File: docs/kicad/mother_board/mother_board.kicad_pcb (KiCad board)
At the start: 2 copper layers, 148 x 92.5 mm, 37 parts, among them J1 ROW_BOARDS, J10 PEDAL1, J11 PEDAL2, J12 PEDAL3, J13 PEDAL4, J14 GUITAR_IN, J15 LINE_OUT, J16 LEDS, J2 ROTARIES, J3 TE_DISPLAY, J4 RPI_DISPLAY, J5 rPi_5V, J6 RPI_RUN, J7 rpi_connector, J8 I2S_TXB, J9 EigthInchJack1, Q1 BC547, U1 teensyAudioRevD_WithAudio, U2 myTeensy4.1

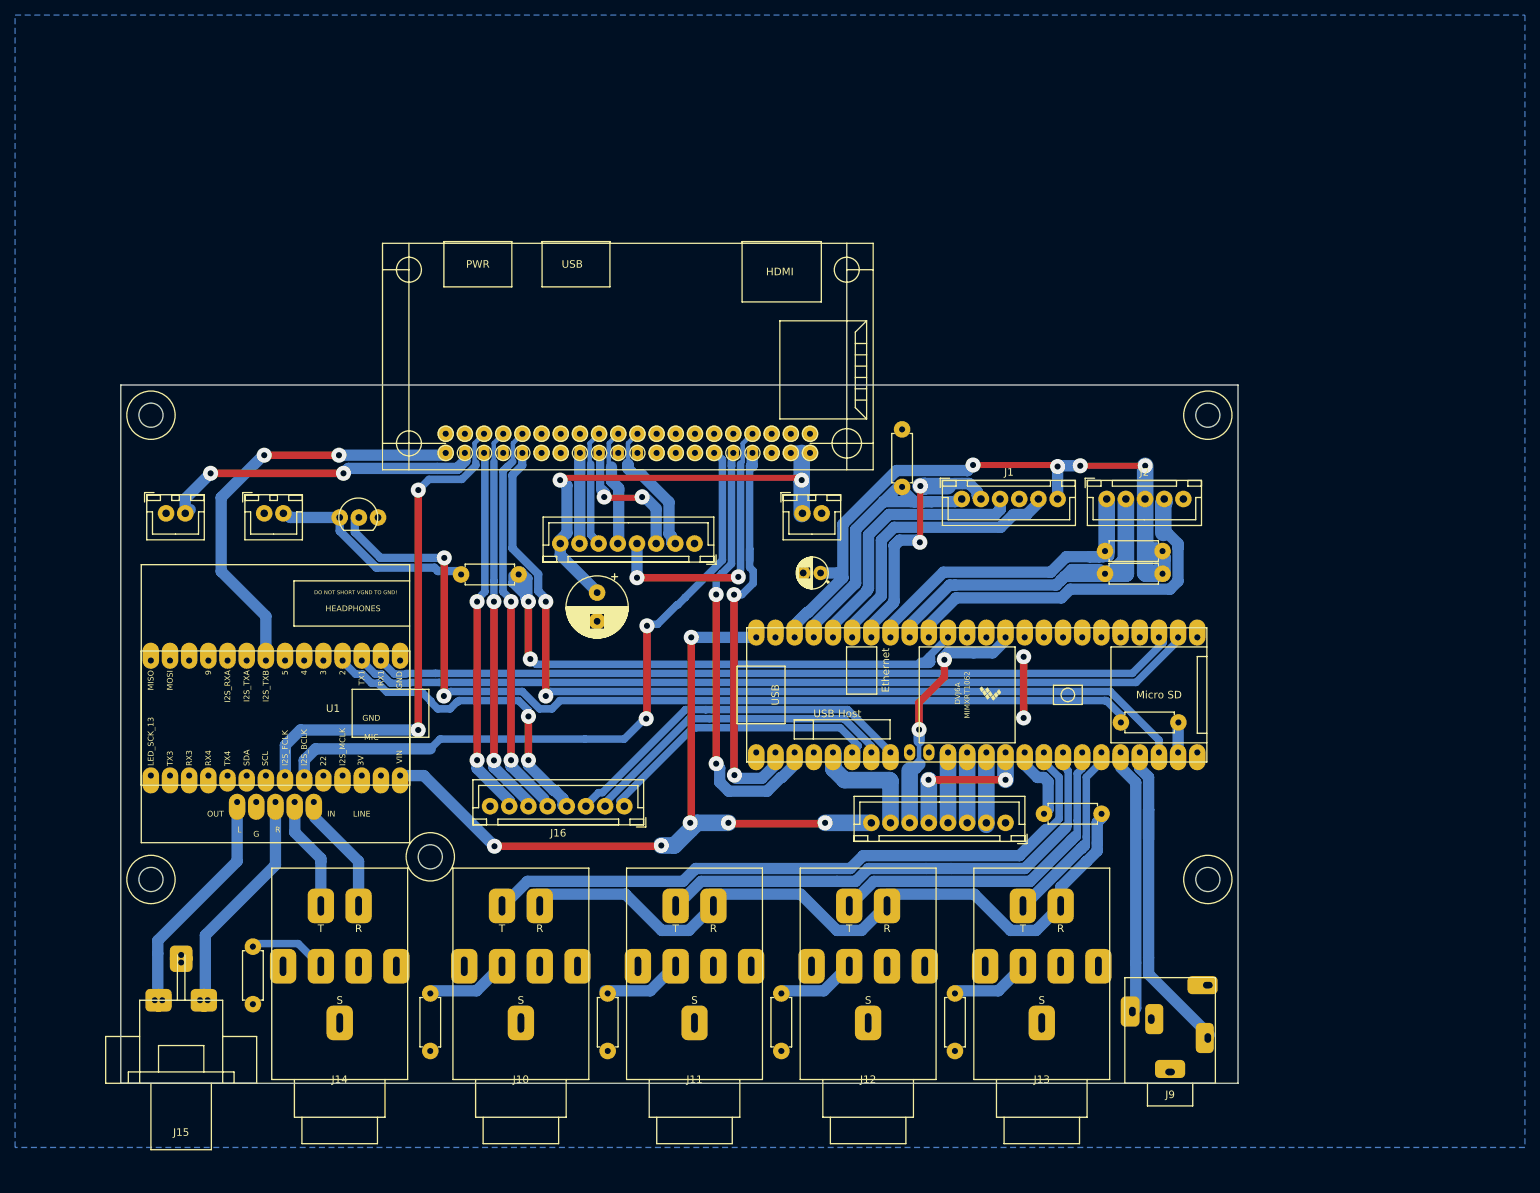
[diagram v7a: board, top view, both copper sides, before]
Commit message: produced and submitted mother_board and row_board to PCBWay for production
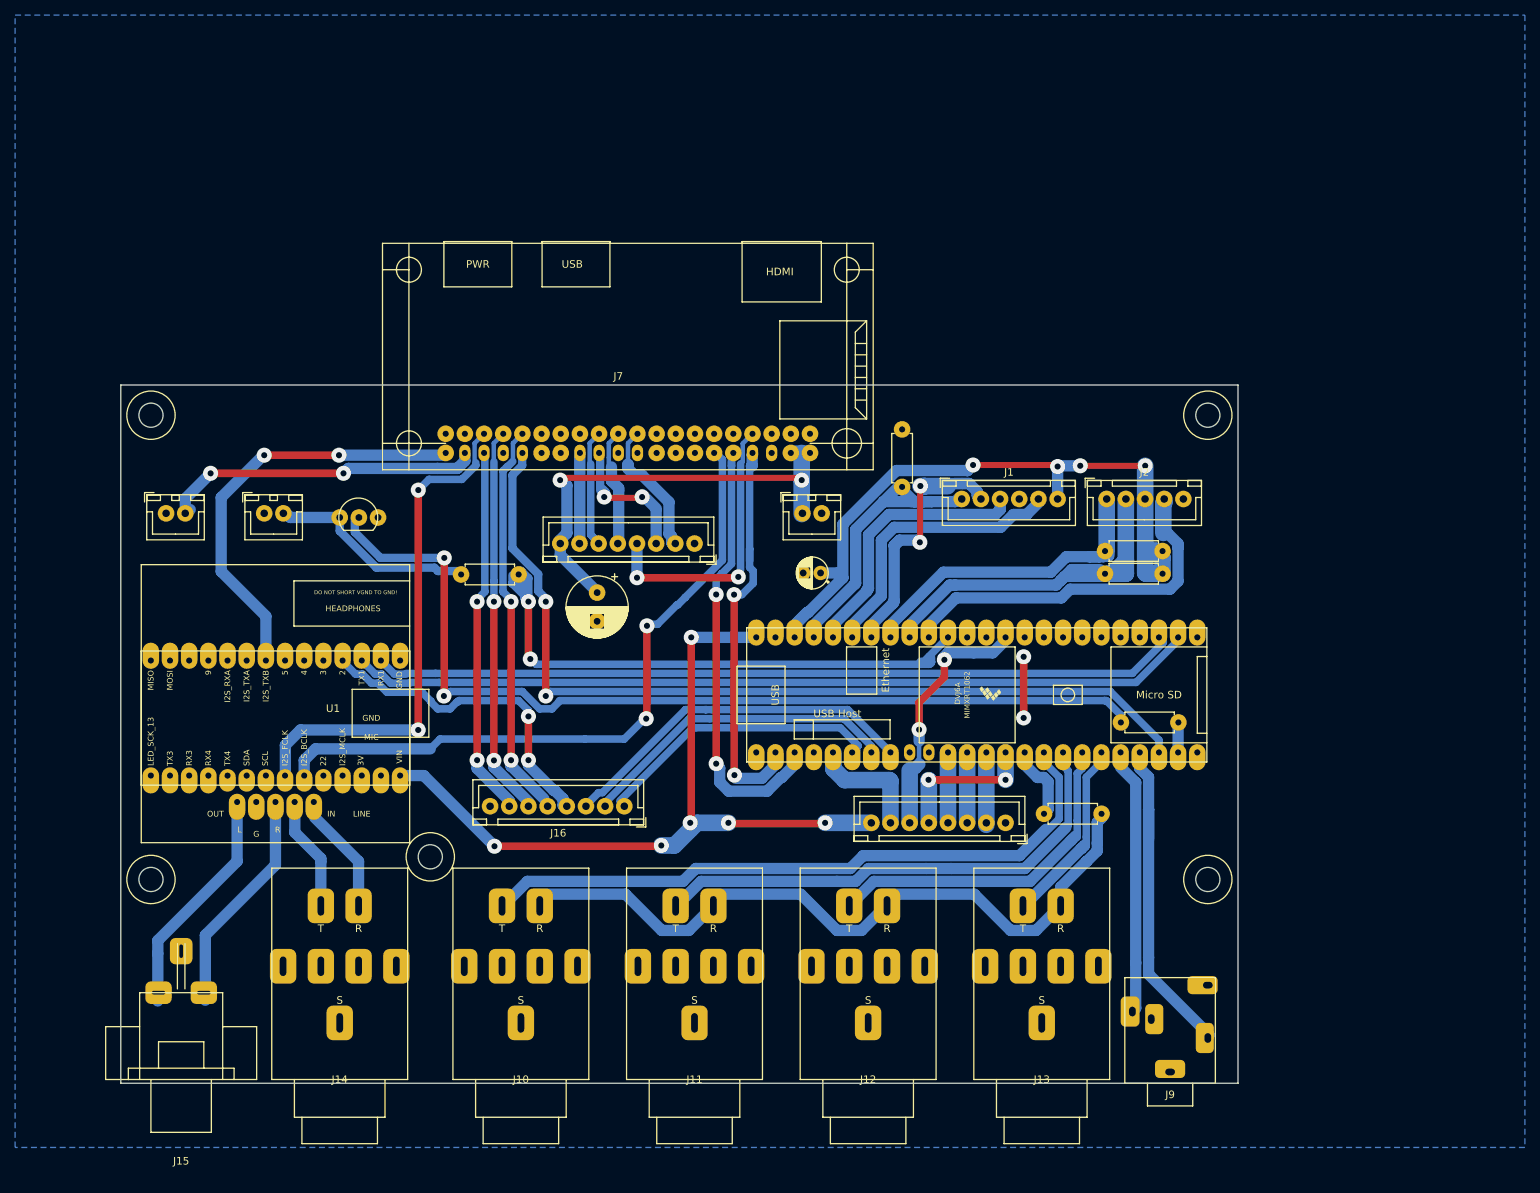
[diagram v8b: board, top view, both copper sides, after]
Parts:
- removed R10, R6, R7, R8, R9: 10K, 0_my_footprints:myResistor
- J15: footprint 0_my_footprints2:RCA2_PCB -> 0_my_footprints2:RCA2_PCB_milled
- J7: footprint 0_my_footprints2:rpi_zero_2w -> 0_my_footprints2:rpi_zero_2w_for_TE3
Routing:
- net Net-(J10-Pad6): track 10.8 -> 0.12 mm
- net Net-(J11-Pad6): track 10.7 -> 0.12 mm
- net Net-(J13-Pad6): track 10.4 -> 0.00 mm
- net Net-(J12-Pad6): track 10.3 -> 0.12 mm
- net Net-(J14-Pad6): track 10.0 -> 0.00 mm
